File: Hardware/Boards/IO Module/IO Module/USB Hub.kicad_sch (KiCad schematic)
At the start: 77 parts, among them U16 TPS74801AWDRC, U18 TUSB8041, U24 TUSB1142, Y4 24Mhz

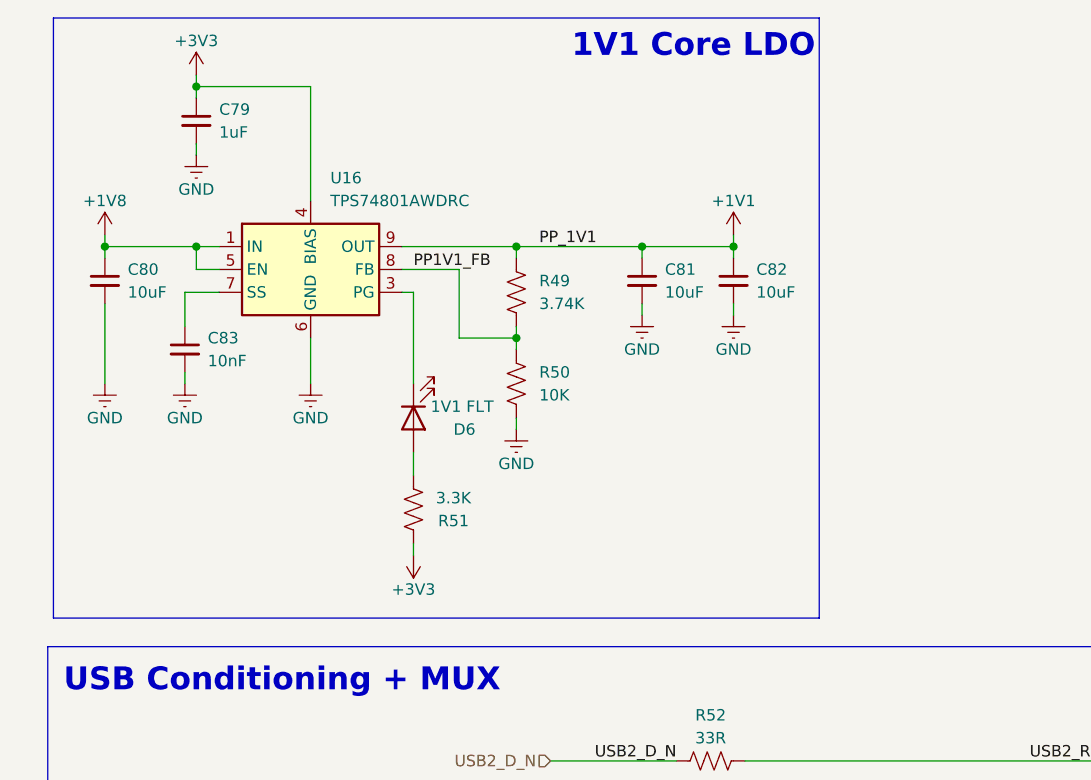
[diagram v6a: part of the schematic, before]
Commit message: Cleaned up IO Module and went through DRC errors
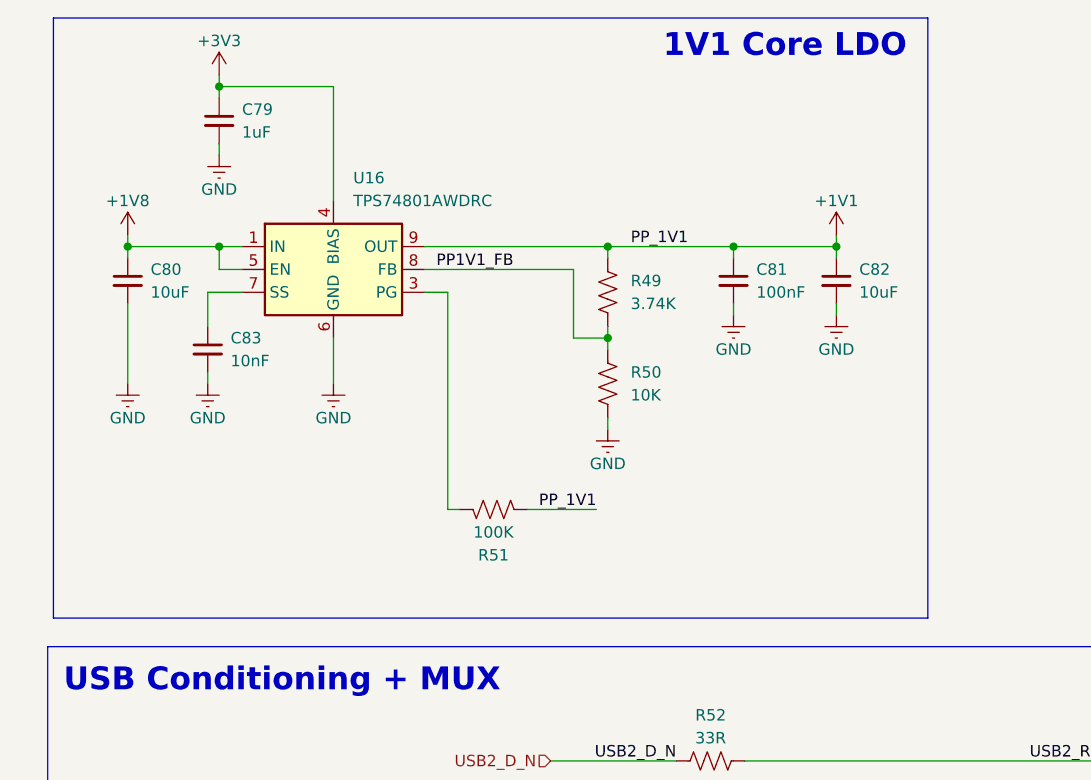
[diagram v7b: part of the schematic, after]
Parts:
- removed D6: 1V1 FLT, LED_SMD:LED_0603_1608Metric, symbol Device:LED
- C81: value 10uF -> 100nF; footprint Capacitor_SMD:C_0603_1608Metric -> Capacitor_SMD:C_0201_0603Metric
- R51: value 3.3K -> 100K
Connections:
- net +1V1: now also R51.1
- net +3V3: no longer R51.1
- net at U16.3 (PG): now also R51.2
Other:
- moved on the sheet: C79, C80, C81, C82, C83, R49, R50, U16

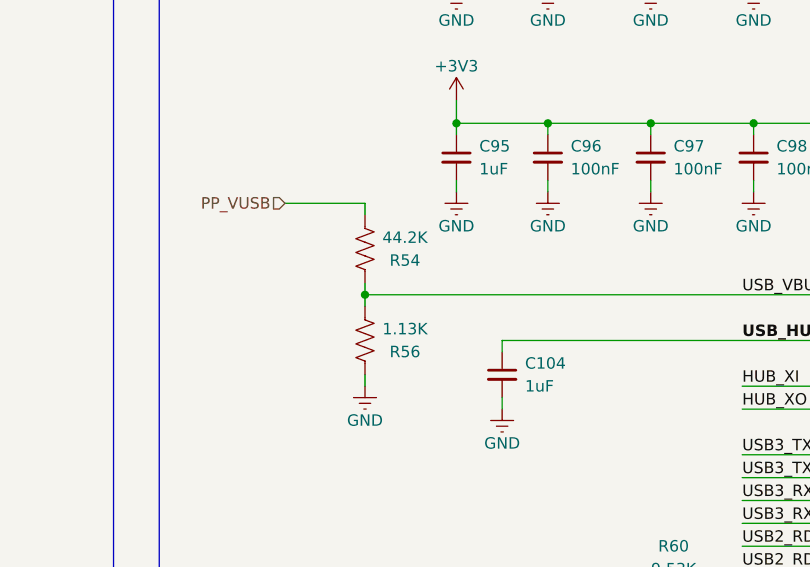
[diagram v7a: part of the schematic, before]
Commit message: Updated SCH and Layout
Added temp sensors for DCDC's, Added MCU control for FPGA mode, removed mode DIP switch
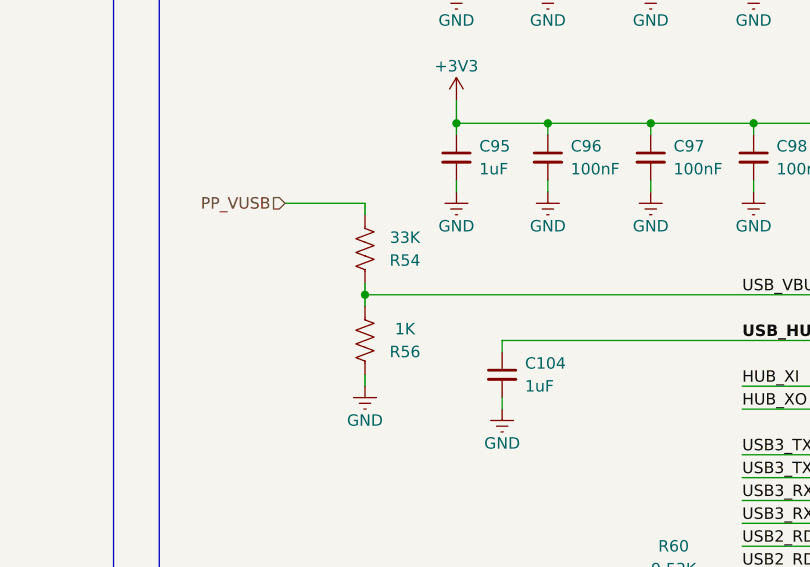
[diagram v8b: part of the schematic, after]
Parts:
- R54: value 44.2K -> 33K
- R56: value 1.13K -> 1K
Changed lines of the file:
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@@
 			)
 		)
-		(property "Value" "1.13K"
+		(property "Value" "1K"
 			(at 200.025 147.32 0)
 			(effects
@@
 			)
 		)
-		(property "Value" "44.2K"
+		(property "Value" "33K"
 			(at 200.025 137.16 0)
 			(effects
